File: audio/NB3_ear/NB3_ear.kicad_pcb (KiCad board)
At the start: 2 copper layers, 20 x 18 mm, 6 parts, among them J1 Conn_02x03_Odd_Even, J2 Conn_02x03_Odd_Even

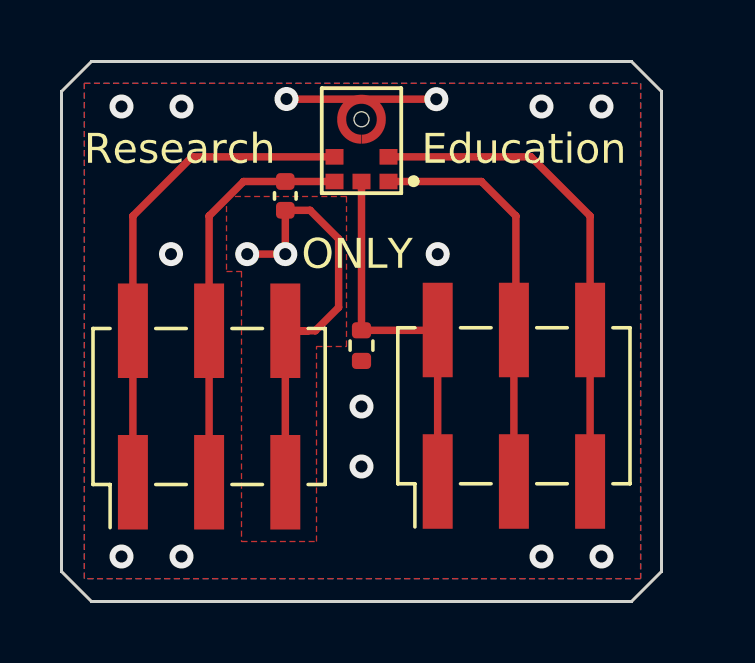
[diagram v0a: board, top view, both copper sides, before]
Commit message: Update PCBs (body, ear, mouth, and power)
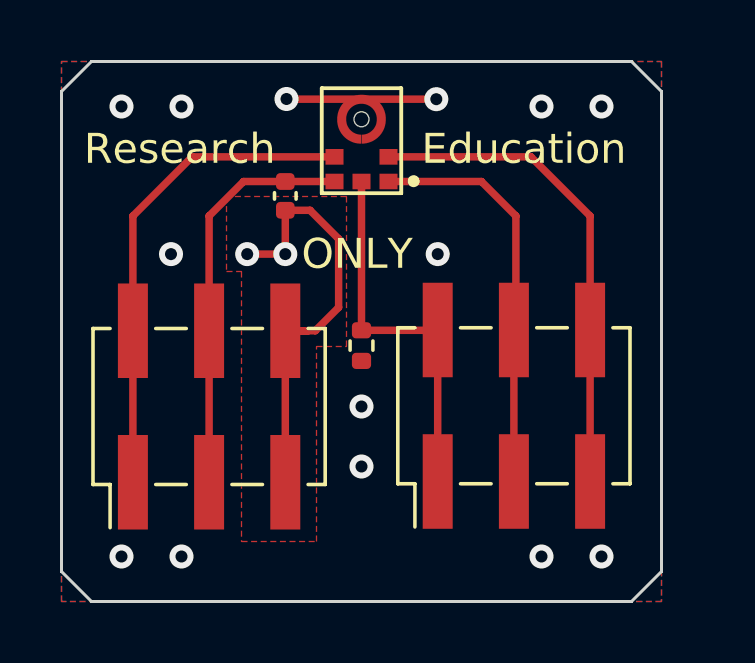
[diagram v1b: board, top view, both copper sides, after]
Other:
- board text added: "NB3 Ear Rev 0.0.3"
- board text removed: "NB3 Ear Rev 0.0.2"
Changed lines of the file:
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@@
   (title_block
     (title "NB3 Ear")
-    (date "2021-07-06")
-    (rev "0.0.1")
+    (date "2023-11-29")
+    (rev "0.0.3")
     (company "Voight-Kampff")
     (comment 1 "MEMS microphone with I2S interface PCB")
@@
     (pad "6" smd rect (at 0 -1.361 180) (size 0.6 0.522) (layers "F.Cu" "F.Mask")
       (net 4 "/SD") (pinfunction "SD") (pintype "output"))
-    (model "${KIPRJMOD}/libraries/parts/Mic_ ICS-43434/Mic_ICS-43434.step"
+    (model "${KIPRJMOD}/libraries/parts/Mic_ICS-43434/Mic_ICS-43434.step"
       (offset (xyz 0 0 0))
       (scale (xyz 1 1 1))
@@
     (effects (font (size 0.8 0.7) (thickness 0.15)) (justify mirror))
   )
-  (gr_text "NB3 Ear\nRev 0.0.2" (at 156.08 102.275) (layer "B.SilkS")
+  (gr_text "NB3 Ear\nRev 0.0.3" (at 156.08 102.275) (layer "B.SilkS")
     (effects (font (size 1 1) (thickness 0.15)) (justify mirror))
   )
@@
     (polygon
       (pts
-        (xy 141.842 99.003)
-        (xy 160.384 99.003)
-        (xy 160.384 115.513)
-        (xy 141.842 115.513)
+        (xy 141.08 98.275)
+        (xy 161.08 98.275)
+        (xy 161.08 116.275)
+        (xy 141.08 116.275)
       )
     )
@@
     (polygon
       (pts
-        (xy 160.384 115.513)
-        (xy 141.842 115.513)
-        (xy 141.842 99.003)
-        (xy 160.384 99.003)
+        (xy 161.08 116.275)
+        (xy 141.08 116.275)
+        (xy 141.08 98.275)
+        (xy 161.08 98.275)
       )
     )
